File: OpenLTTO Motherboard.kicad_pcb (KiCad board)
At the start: 2 copper layers, 60 x 60 mm, 17 parts, among them J1 MBUS, Q1 IRLML6244

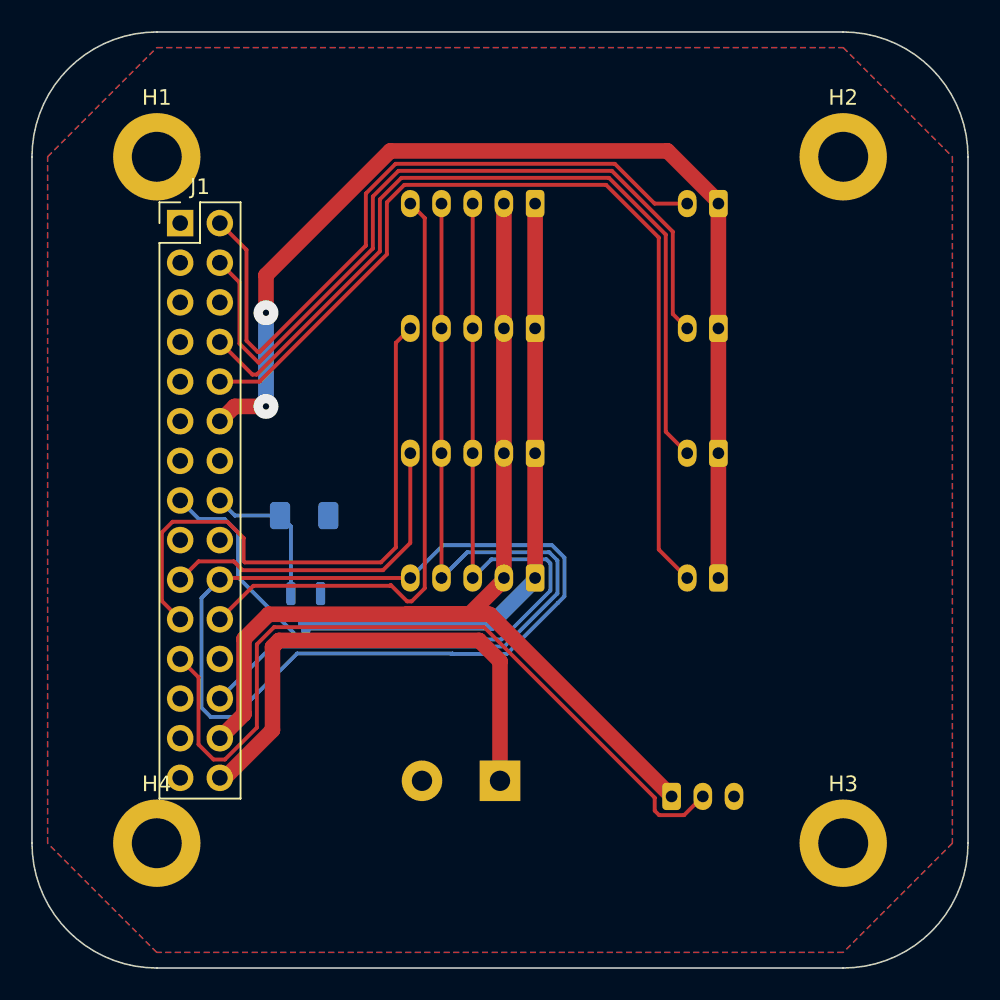
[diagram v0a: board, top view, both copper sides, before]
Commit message: Updated Schematic to v1.1, added GPIO breakout and changed IR ports to all be independent. Also added I2C port, and added license, and updated readme
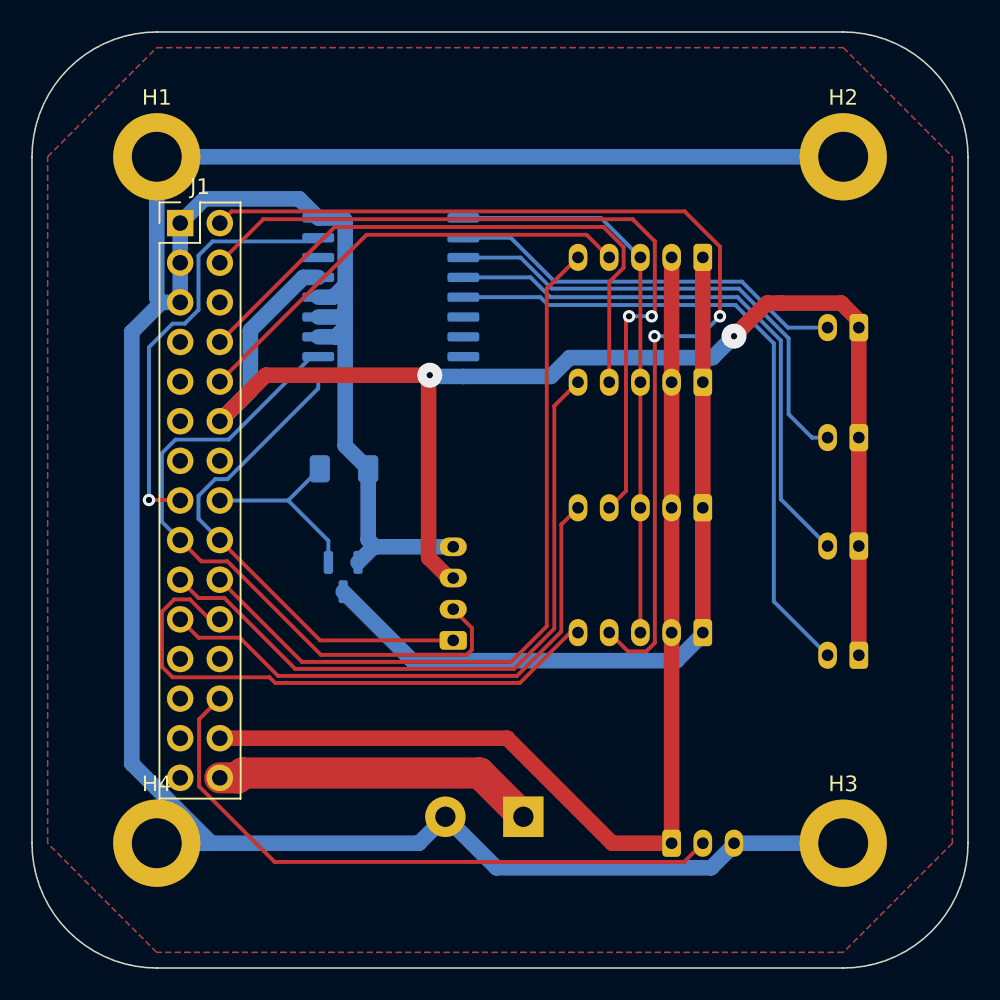
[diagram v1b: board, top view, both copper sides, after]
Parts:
- added I2C1: ~, Connector_JST:JST_PH_B4B-PH-K_1x04_P2.00mm_Vertical, B.Cu at (148.0, 107.0)
- added REF**: OSHW-Logo2_9.8x8mm_SilkScreen, Symbol:OSHW-Logo2_9.8x8mm_SilkScreen, B.Cu at (139.0, 121.0)
- added U1: MCP23008-xSO, Package_SO:SOIC-18W_7.5x11.6mm_P1.27mm, B.Cu at (144.0, 85.0)
- moved SW4 30.3 mm to (174.0, 108.0)
- moved IR4 29.5 mm to (164.0, 106.5)
- moved IR1 23.2 mm to (164.0, 82.5)
- moved SW1 18.4 mm to (174.0, 87.0)
- moved SW3 16.6 mm to (174.0, 101.0)
- moved IR3 15.7 mm to (164.0, 98.5)
- moved IR2 11.7 mm to (164.0, 90.5)
- moved SW2 9.06 mm to (174.0, 94.0)
- moved R1 3.94 mm to (141.0, 96.0)
- moved Q1 3.12 mm to (140.9, 102.9)
- moved RGB1 3.00 mm to (162.0, 120.0)
- moved BATT1 2.75 mm to (152.5, 118.3)
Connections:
- IR1 pad 4: /IR_TX -> /IR_TX_A
- IR2 pad 4: /IR_TX -> /IR_TX_B
- IR3 pad 4: /IR_TX -> /IR_TX_C
- IR4 pad 4: /IR_TX -> /IR_TX_D
- J1 pad 10: /GPIO_BTN_A -> /IR_TX_A
- J1 pad 15: /IR_MODE -> /MCP23008_INT
- J1 pad 17: unconnected-(J1-Pin_17-Pad17) -> /MBUS_SYS_SDA
- J1 pad 18: unconnected-(J1-Pin_18-Pad18) -> /MBUS_SYS_SCL
- J1 pad 2: /GPIO_BTN_D -> /IR_TX_D
- J1 pad 23: /RGB_D -> unconnected-(J1-Pin_23-Pad23)
- J1 pad 26: /IR_TX -> /RGB_D
- J1 pad 4: /GPIO_BTN_C -> /IR_TX_C
- J1 pad 8: /GPIO_BTN_B -> /IR_TX_B
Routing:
- net GND: track 0.00 -> 193.5 mm
- net /IR_TX_D: track 0.00 -> 65.8 mm, vias 0 -> 2
- net /IR_TX: track 59.6 -> 0.00 mm
- net /IR_TX_C: track 0.00 -> 48.8 mm, vias 0 -> 2
- net /MBUS_SYS_SDA: track 0.00 -> 43.6 mm
- net /IR_TX_B: track 0.00 -> 38.5 mm
- net /GPIO_BTN_A: track 59.3 -> 25.7 mm
- net /MBUS_SYS_SCL: track 0.00 -> 32.3 mm
- net /IR_TX_A: track 0.00 -> 29.5 mm
- net /MCP23008_INT: track 0.00 -> 27.6 mm, vias 0 -> 1
- net /IR_MODE: track 61.7 -> 36.4 mm
- net +3V3: track 69.5 -> 92.3 mm
- net /IR_RX_B: track 21.9 -> 43.8 mm
- net /GPIO_BTN_B: track 52.7 -> 31.0 mm
- net /IR_RX_A: track 61.4 -> 48.6 mm
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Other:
- board text added: "OpenLTTO Motherboard V1.1"
